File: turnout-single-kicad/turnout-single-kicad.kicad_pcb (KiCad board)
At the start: 2 copper layers, 29 x 24 mm, 16 parts

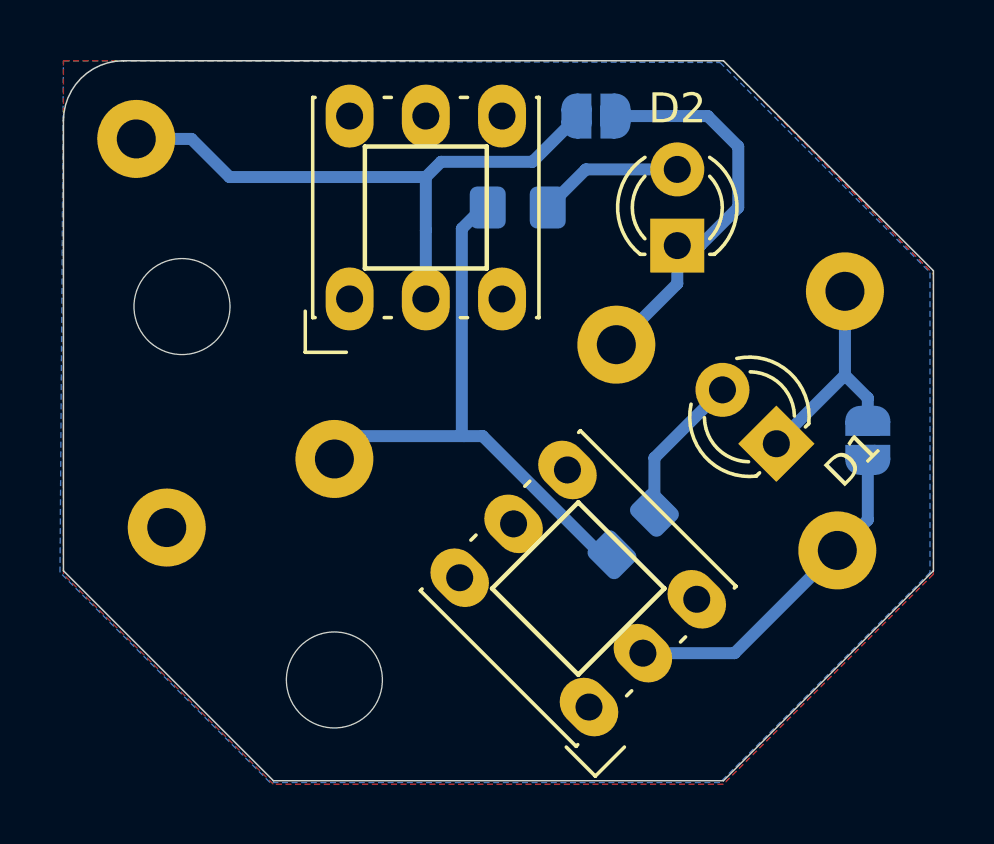
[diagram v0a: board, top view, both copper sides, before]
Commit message: turnout-single: update to KiCad 6.
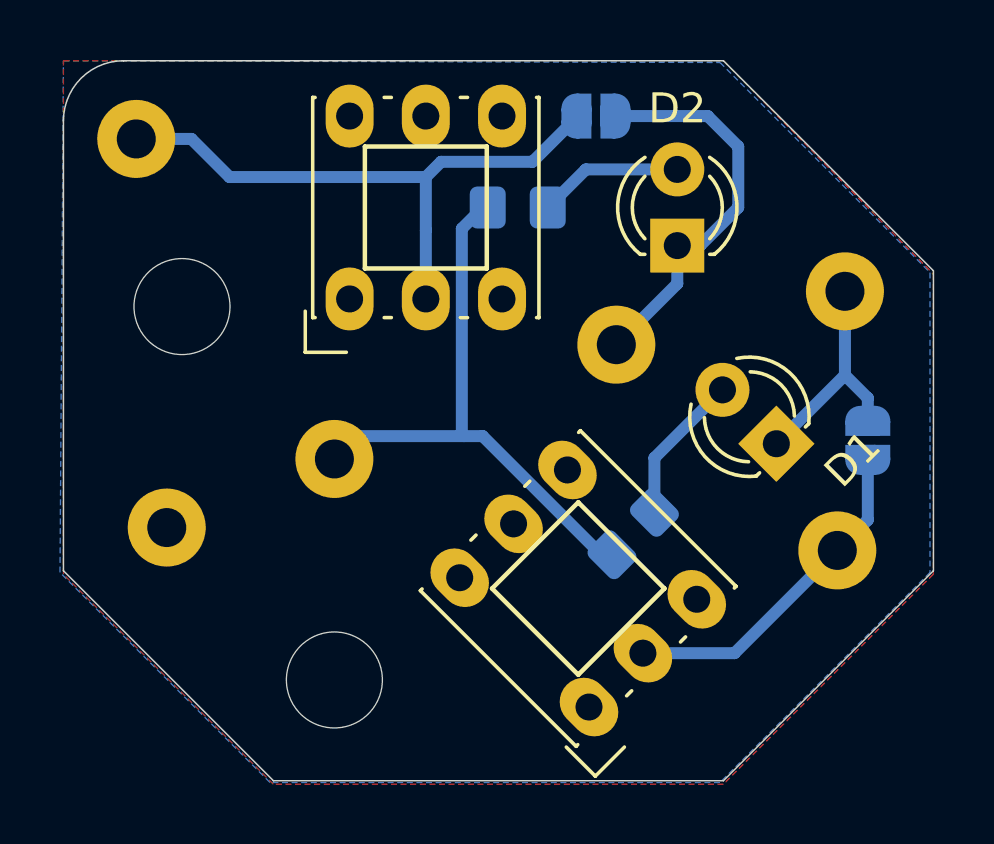
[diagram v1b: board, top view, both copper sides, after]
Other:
- net class Default removed
